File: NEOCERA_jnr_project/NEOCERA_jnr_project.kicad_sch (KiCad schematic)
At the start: 0 parts

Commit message: microcontroller
microcontroller
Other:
- added sheet microcontroller (micro.kicad_sch)
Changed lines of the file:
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@@
+	)
+	(sheet
+		(at 193.04 39.37)
+		(size 49.53 34.29)
+		(fields_autoplaced yes)
+		(stroke
+			(width 0.1524)
+			(type solid)
+		)
+		(fill
+			(color 0 0 0 0.0000)
+		)
+		(property "Sheetname" "microcontroller"
+			(at 193.04 38.6584 0)
+			(effects
+				(font
+					(size 1.27 1.27)
+				)
+				(justify left bottom)
+			)
+		)
+		(property "Sheetfile" "micro.kicad_sch"
+			(at 193.04 74.2446 0)
+			(effects
+				(font
+					(size 1.27 1.27)
+				)
+				(justify left top)
+			)
+		)
+		(instances
+			(project "NEOCERA_jnr_project"
+				(path "/a8746ab6-0163-416c-99f9-0036ded73fc6"
+					(page "8")
+				)
+			)
+		)
 	)
 	(sheet

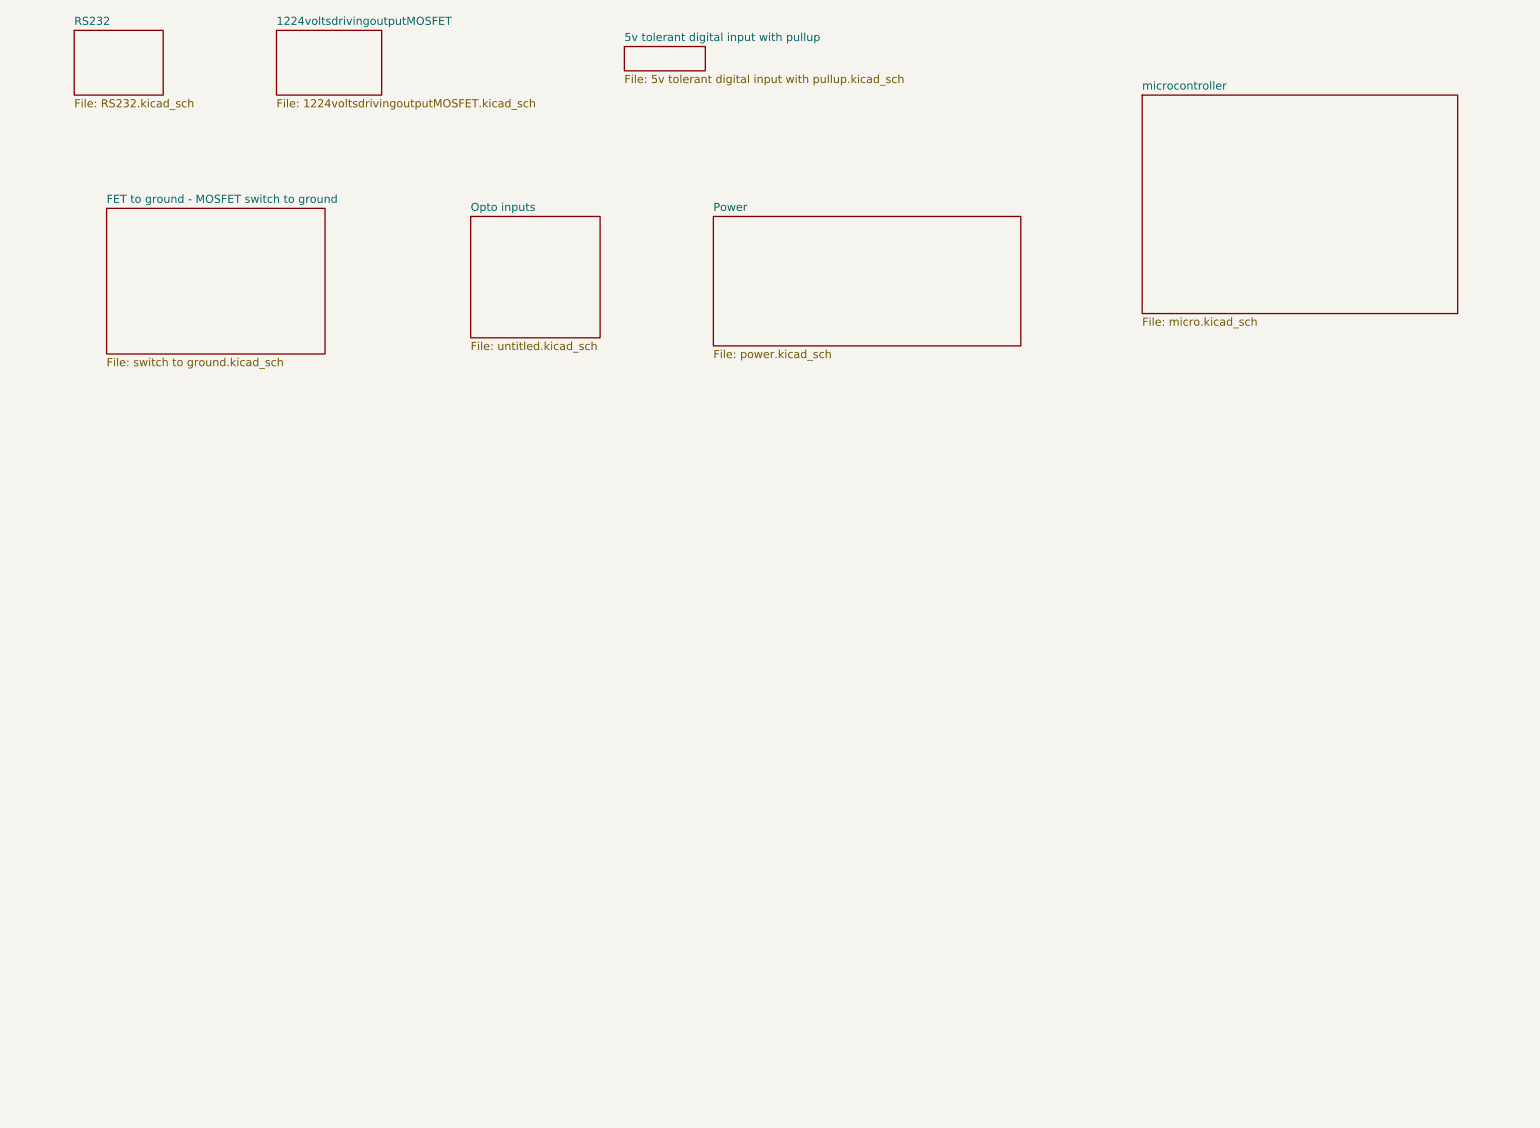
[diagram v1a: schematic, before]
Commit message: Edits made with Dr. Caw.
I added the net to the root
I added the write global nets to some of the previously designed symbols like TX/RX
I added a 3.3V pullup resistor to the opto
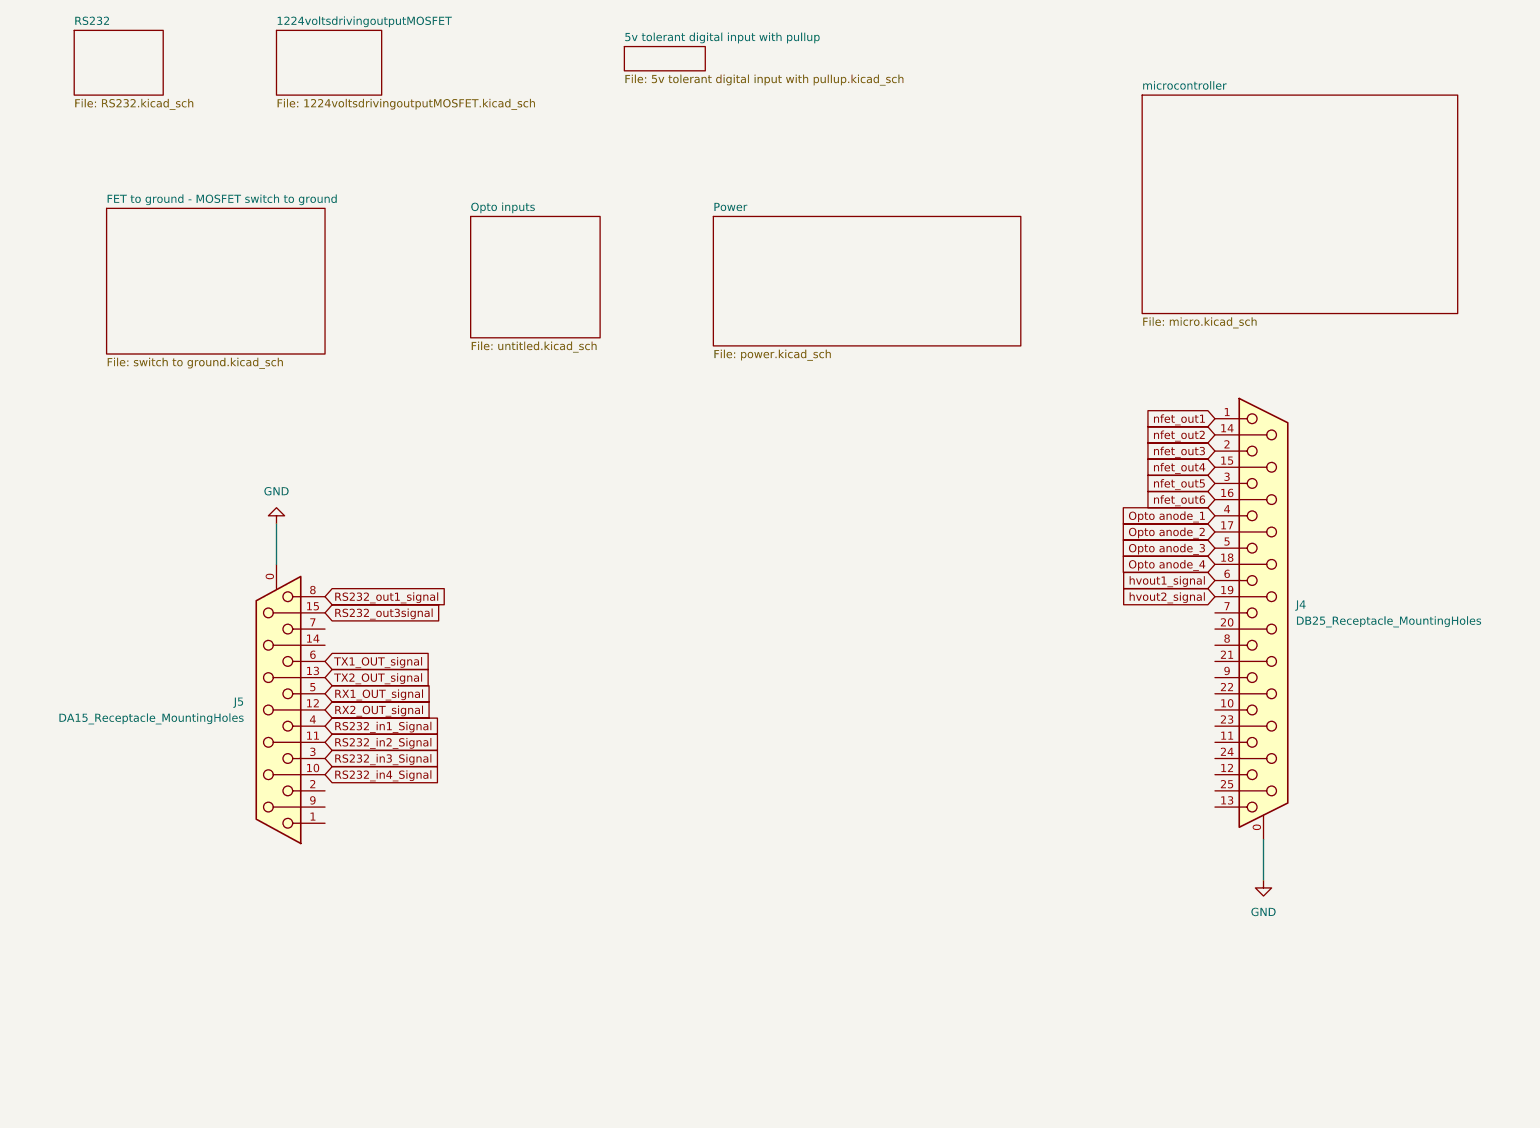
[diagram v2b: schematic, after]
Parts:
- added J4: DB25_Receptacle_MountingHoles, symbol Connector:DB25_Receptacle_MountingHoles
- added J5: DA15_Receptacle_MountingHoles, symbol Connector:DA15_Receptacle_MountingHoles
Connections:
- new net GND: J4.0 (PAD), J5.0 (PAD)
- new net Opto anode_1: J4.4
- new net Opto anode_2: J4.17 (P17)
- new net Opto anode_3: J4.5
- new net Opto anode_4: J4.18 (P18)
- new net RS232_in1_Signal: J5.4
- new net RS232_in2_Signal: J5.11 (P111)
- new net RS232_in3_Signal: J5.3
- new net RS232_in4_Signal: J5.10 (P10)
- new net RS232_out1_signal: J5.8
- new net RS232_out3signal: J5.15 (P15)
- new net RX1_OUT_signal: J5.5
- new net RX2_OUT_signal: J5.12 (P12)
- new net TX1_OUT_signal: J5.6
- new net TX2_OUT_signal: J5.13 (P13)
- new net hvout1_signal: J4.6
- new net hvout2_signal: J4.19 (P19)
- new net nfet_out1: J4.1
- new net nfet_out2: J4.14 (P14)
- new net nfet_out3: J4.2
- new net nfet_out4: J4.15 (P15)
- new net nfet_out5: J4.3
- new net nfet_out6: J4.16 (P16)

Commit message: bunch of edits
bunch of edits were done including DB37
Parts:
- removed J4: DB25_Receptacle_MountingHoles, symbol Connector:DB25_Receptacle_MountingHoles
- removed J5: DA15_Receptacle_MountingHoles, symbol Connector:DA15_Receptacle_MountingHoles
- added J6: DC37_Receptacle_MountingHoles, symbol Connector:DC37_Receptacle_MountingHoles
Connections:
- net GND: now also J6.0 (PAD), J6.15, J6.2, J6.20, J6.33
- net Opto anode_1: now also J6.30
- net Opto anode_2: now also J6.12
- net Opto anode_3: now also J6.31
- net Opto anode_4: now also J6.13
- net RS232_in1_Signal: now also J6.4
- net RS232_in2_Signal: now also J6.22
- net RS232_in3_Signal: now also J6.3
- net RS232_in4_Signal: now also J6.21
- net RS232_out1_signal: now also J6.8
- net RS232_out3signal: now also J6.26
- new net +24V: J6.14
- new net +3.3V: J6.1
- new net +5V: J6.34
- new net DO1: J6.23
- new net DO2: J6.5
- new net DO3: J6.24
- new net DO4: J6.6
- new net DO5: J6.25
- new net DO6: J6.7
- new net hvcontrol1_in: J6.16
- new net hvcontrol2_in: J6.35
- new net hvcontrol3_in: J6.17
- new net hvcontrol4_in: J6.36
- new net nfet_in1: J6.27
- new net nfet_in2: J6.9
- new net nfet_in3: J6.28
- new net nfet_in4: J6.10
- new net nfet_in5: J6.29
- new net nfet_in6: J6.11

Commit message: bunch
bunch
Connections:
- net Opto anode_1 is gone; now on net opto_output4: J6.30
- net Opto anode_2 is gone; now on net opto_output3: J6.12
- net Opto anode_3 is gone; now on net opto_output2: J6.31
- net Opto anode_4 is gone; now on net opto_output1: J6.13
- net RS232_in1_Signal is gone; now on net TX1_OUT_signal: J6.4
- net RS232_in2_Signal is gone; now on net TX2_OUT_signal: J6.22
- net RS232_in3_Signal is gone; now on net RX1_OUT_signal: J6.3
- net RS232_in4_Signal is gone; now on net RX2_OUT_signal: J6.21
- net nfet_in1 is gone; now on net nfet_out1: J6.27
- net nfet_in2 is gone; now on net nfet_out2: J6.9
- net nfet_in3 is gone; now on net nfet_out3: J6.28
- net nfet_in4 is gone; now on net nfet_out4: J6.10
- net nfet_in5 is gone; now on net nfet_out5: J6.29
- net nfet_in6 is gone; now on net nfet_out6: J6.11
- net +24V: now also J6.32
- net +5V: now also J6.18
- net DO1 renamed D_IN1_out
- net DO2 renamed D_IN2_out
- net DO3 renamed D_IN3_out
- net DO4 renamed D_IN4_out
- net DO5 renamed D_IN5_out
- net DO6 renamed D_IN6_out
- net hvcontrol1_in renamed hvout1_mboard
- net hvcontrol2_in renamed hvout2_mboard
- net hvcontrol3_in renamed hvout3_mboard
- net hvcontrol4_in renamed hvout4_mboard

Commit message: symbols changed
edited all symbols
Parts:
- J6: footprint (none) -> Connector_Dsub:DSUB-37_Female_Horizontal_P2.77x2.84mm_EdgePinOffset7.70mm_Housed_MountingHolesOffset9.12mm
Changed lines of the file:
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@@
 			)
 		)
-		(property "Footprint" ""
+		(property "Footprint" "Connector_Dsub:DSUB-37_Female_Horizontal_P2.77x2.84mm_EdgePinOffset7.70mm_Housed_MountingHolesOffset9.12mm"
 			(at 144.78 135.89 0)
 			(effects
